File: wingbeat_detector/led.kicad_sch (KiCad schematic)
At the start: 1 part

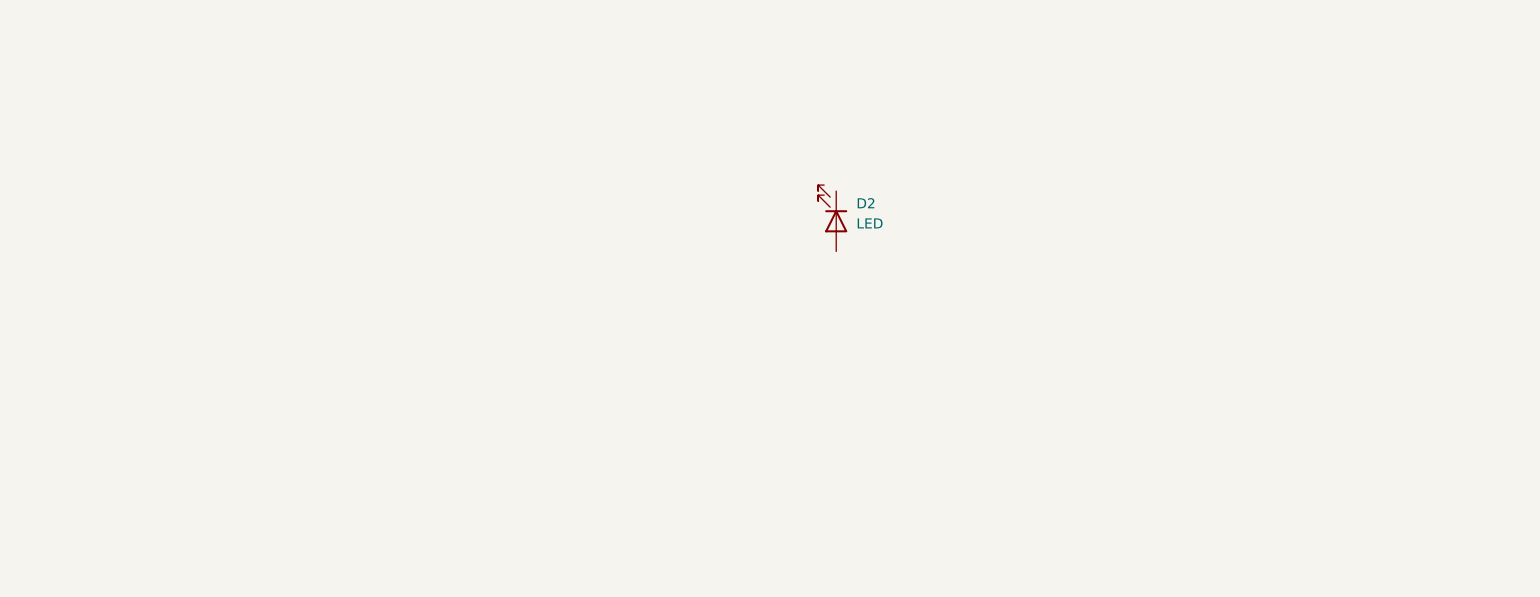
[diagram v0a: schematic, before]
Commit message: Add led driver
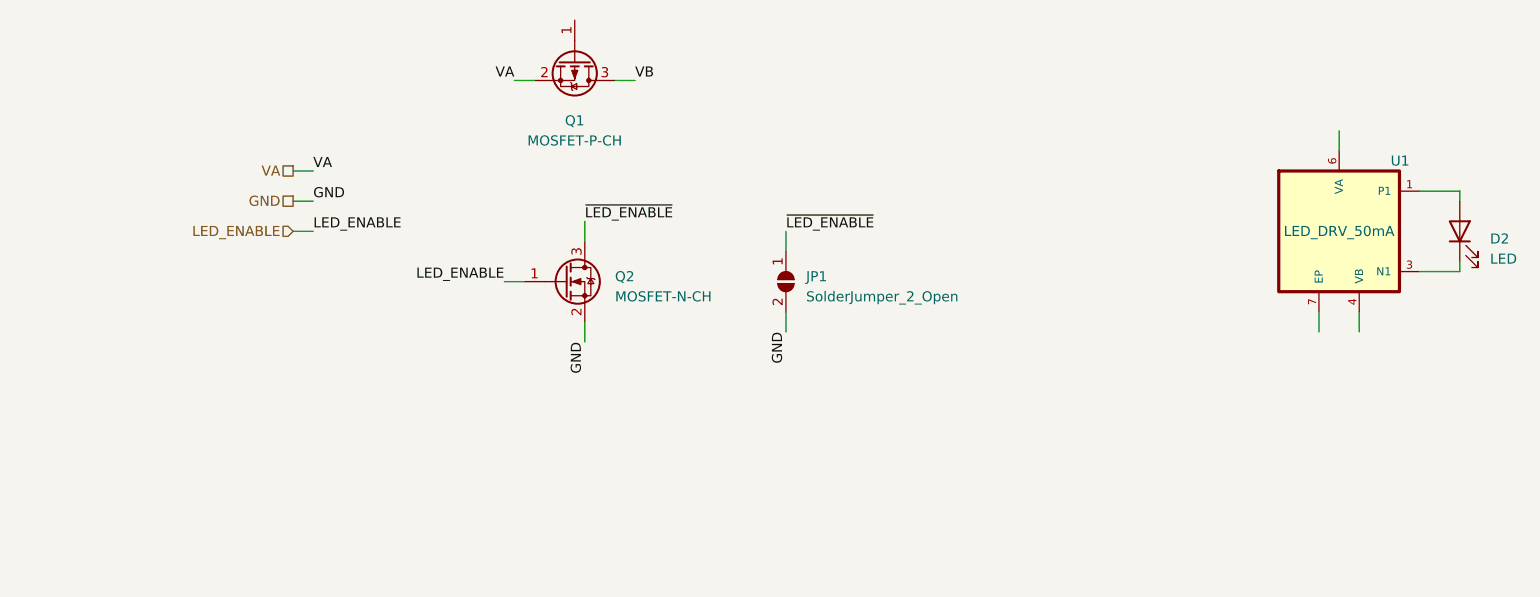
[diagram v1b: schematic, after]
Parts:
- added JP1: SolderJumper_2_Open, Janelia:SolderJumper-2_P1.3mm_Open_RoundedPad1.0x1.5mm, symbol Janelia:SolderJumper_2_Open
- added Q1: MOSFET-P-CH, Janelia:SOT-23-3, symbol Janelia:MOSFET-P-CH-EN-DMP2045UQ-7
- added Q2: MOSFET-N-CH, Janelia:SOT-23-3, symbol Janelia:MOSFET-N-CH-EN-DMG2302UKQ-7
- added U1: LED_DRV_50mA, Janelia:DFN-6-1EP_2x2mm_P0.65mm_EP1x1.6mm, symbol Janelia:LED_DRIVER_50mA
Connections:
- net at D2.1 (K): now also U1.3 (N1)
- net at D2.2 (A): now also U1.1 (P1)
- new net GND: JP1.2 (B), Q2.2 (S)
- new net LED_ENABLE: Q2.1 (G)
- new net VA: Q1.2 (S)
- new net VB: Q1.3 (D)
- new net ~{LED_ENABLE}: JP1.1 (A), Q2.3 (D)
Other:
- moved on the sheet: D2

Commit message: Add mosfet and opa381
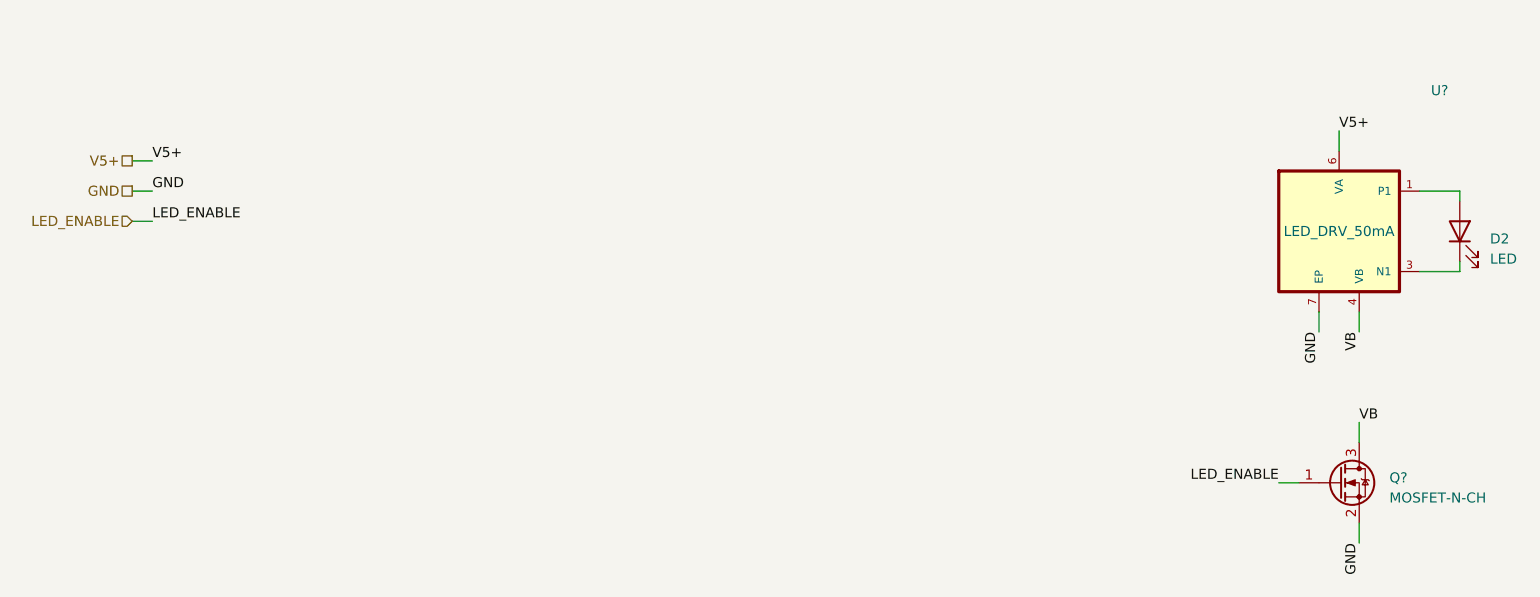
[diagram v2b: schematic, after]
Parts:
- removed JP1: SolderJumper_2_Open, Janelia:SolderJumper-2_P1.3mm_Open_RoundedPad1.0x1.5mm, symbol Janelia:SolderJumper_2_Open
- removed Q1: MOSFET-P-CH, Janelia:SOT-23-3, symbol Janelia:MOSFET-P-CH-EN-DMP2045UQ-7
- removed Q2: MOSFET-N-CH, Janelia:SOT-23-3, symbol Janelia:MOSFET-N-CH-EN-DMG2302UKQ-7
- added Q?: MOSFET-N-CH, Janelia:XFDFN-3, symbol Janelia:MOSFET-N-CH-EN-CSD17483F4
- renumbered U1 to U?
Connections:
- net GND: now also U?.7 (EP), Q?.2 (S)
- net LED_ENABLE: now also Q?.1 (G)
- net VB: now also U?.4 (VB), Q?.3 (D)
- net V5+: now reaches U?.6 (VA)

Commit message: Remove connectors schematic sheet
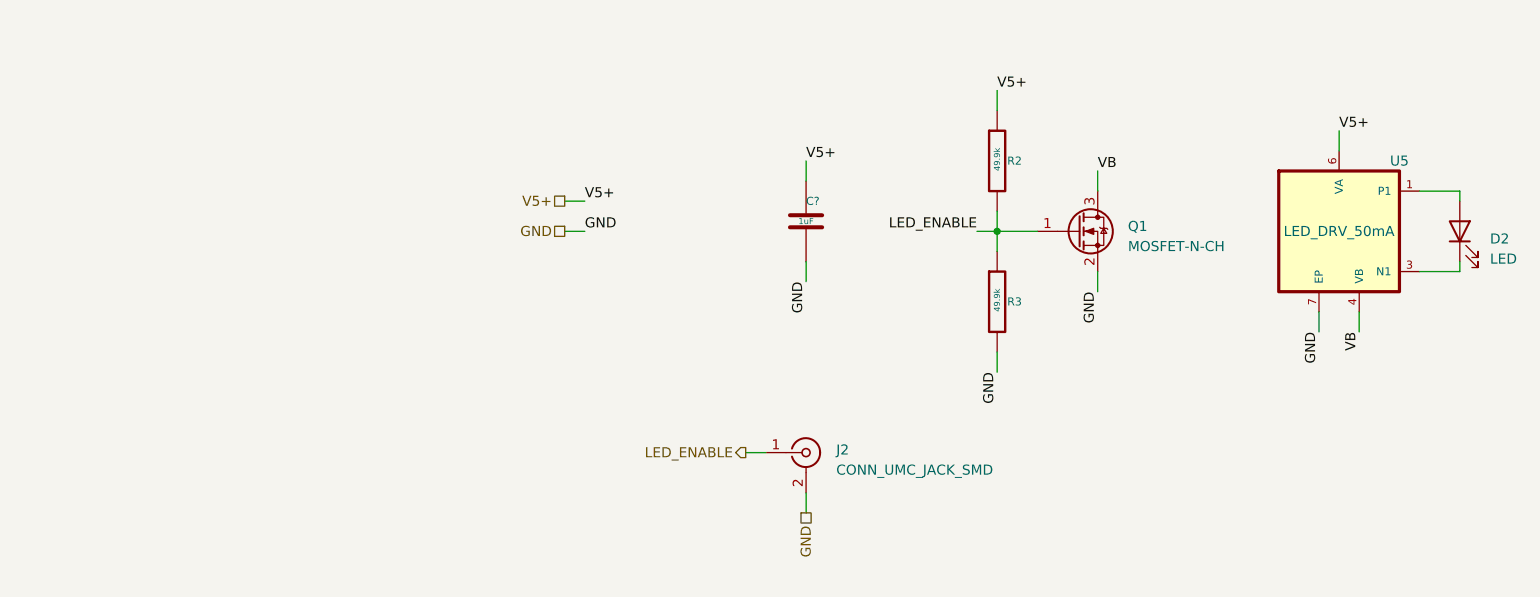
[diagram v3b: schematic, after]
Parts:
- added C?: 1uF, Janelia:C_0402_1005Metric, symbol Janelia:C_1uF_0402
- added J2: CONN_UMC_JACK_SMD, Janelia:UMC_AMPHENOL_A-1JB, symbol Janelia:CONN_UMC_JACK_SMD
- added R2, R3: 49.9k, Janelia:R_0402_1005Metric, symbol Janelia:R_49.9k_0402
- gave numbers to parts that had none: 2
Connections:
- net GND: now also C?.2, J2.2 (Ext), R3.2
- net LED_ENABLE: now also J2.1 (In), R2.2, R3.1
- net V5+: now also C?.1, R2.1
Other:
- moved on the sheet: Q1

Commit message: Add buffered output
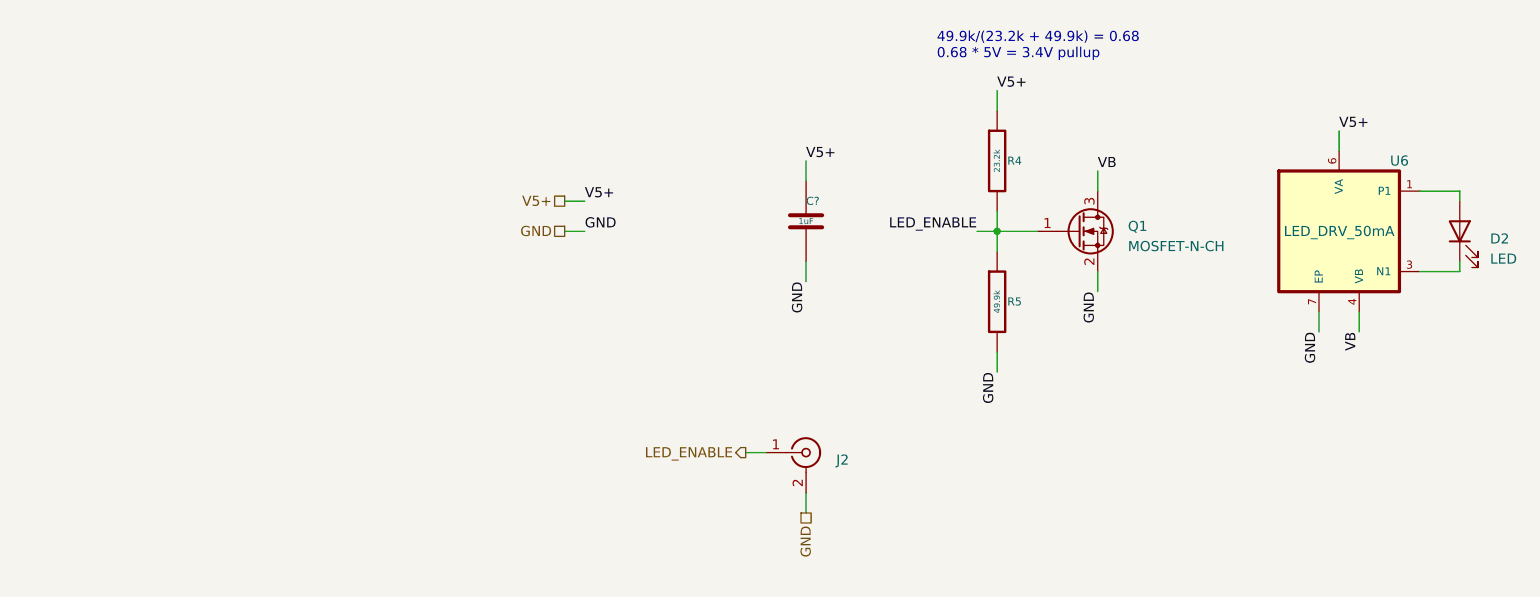
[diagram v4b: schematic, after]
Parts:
- removed R2, R3: 49.9k, Janelia:R_0402_1005Metric, symbol Janelia:R_49.9k_0402
- added R4: 23.2k, Janelia:R_0402_1005Metric, symbol Janelia:R_23.2k_0402
- added R5: 49.9k, Janelia:R_0402_1005Metric, symbol Janelia:R_49.9k_0402
- renumbered U5 to U6
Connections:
- net GND: now also R5.2
- net LED_ENABLE: now also R4.2, R5.1
- net V5+: now also R4.1
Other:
- note added: "49.9k/(23.2k + 49.9k) = 0.68 0.68 * 5V = 3.4V pullup"
- company: (none) -> Howard Hughes Medical Institute
- title: (none) -> wingbeat_detector
